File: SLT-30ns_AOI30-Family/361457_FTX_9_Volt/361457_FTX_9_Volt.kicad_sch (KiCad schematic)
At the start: 5 parts, among them T1 ACB, T2 ACB, T3 ACB, T4 ACB, U1 12-Pin_SLx_Can

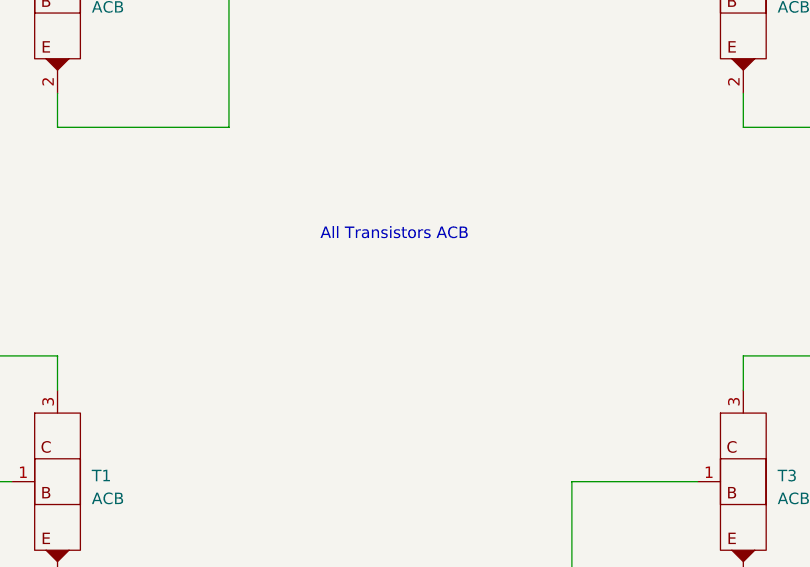
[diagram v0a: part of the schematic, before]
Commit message: Update schematic pdfs
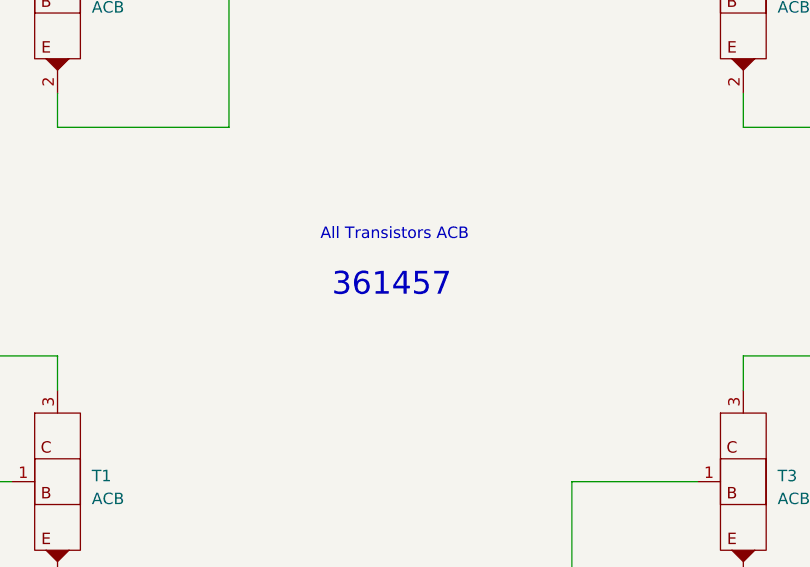
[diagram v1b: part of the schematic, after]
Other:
- note added: "361457"
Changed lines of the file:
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@@
     (stroke (width 0) (type default) (color 0 0 0 0))
+  )
+  (text "361457" (at 119.38 107.95 0)
+    (effects (font (size 2.54 2.54)) (justify left bottom))
   )
   (text "All Transistors ACB" (at 118.11 101.6 0)
